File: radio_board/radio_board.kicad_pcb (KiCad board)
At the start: 2 copper layers, 61.7 x 46.5 mm, 95 parts, among them J1 3.3v, J2 GND, J3 RESET, J4 SWDCLK, J5 SWDIO, Q1 2N7002K, SW2 RKB2SJG250SMTRLFS, SW3 MSK12C02, U1 FSC-BT1036C, U2 TP4057, U3 XB5352A, U5 S2B-PH-K-S(LF)(SN), U6 TLV75533PDBVR, U7 LMV321, U8 STM32G030F6P6TR

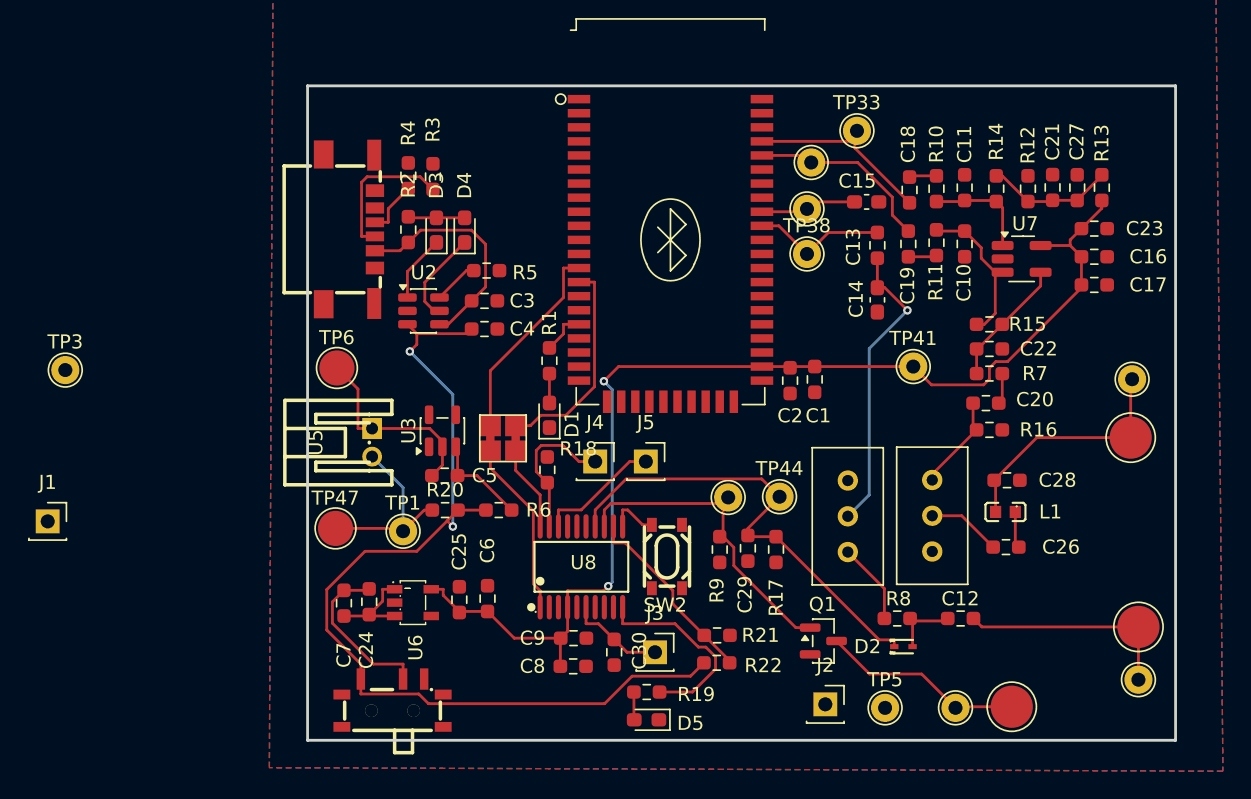
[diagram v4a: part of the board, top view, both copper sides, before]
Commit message: [Feature] Cleaned up PCB and schematics. Add logo, checked schematic, layout and wiring
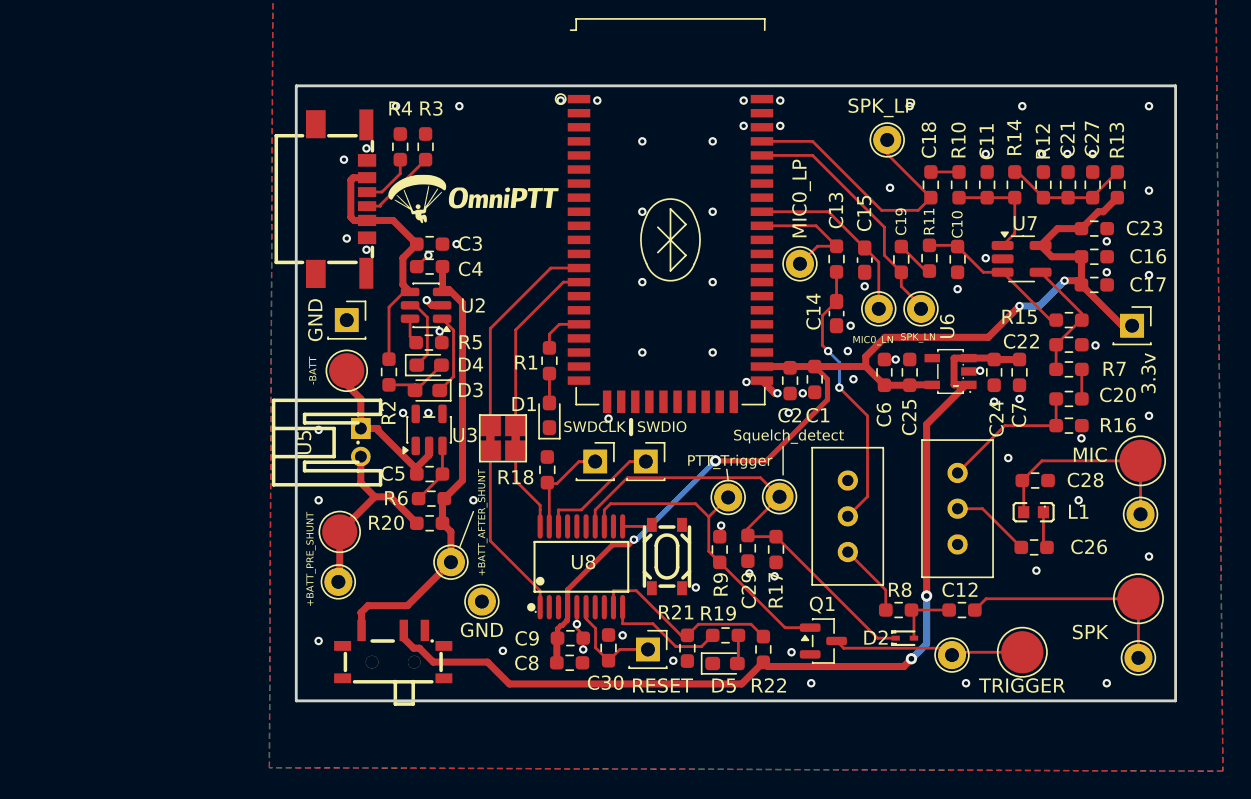
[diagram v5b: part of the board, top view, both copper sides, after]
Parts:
- removed TP41: +3.3V, TestPoint:TestPoint_THTPad_D2.0mm_Drill1.0mm
- added G***: LOGO, PTT_Project_logo:omniPTT_logo, F.Cu at (108.4, 57.0)
- C5: value 0.1uF -> 100nF
- R20: value 1 -> 0.2
- TP1: value TP_IBATT_H -> +BATT_PRE_SHUNT
- TP14, TP43: value K_CONNECTOR_PTT_TRIGGER_SLEEVE -> TRIGGER
- TP20, TP45: value K_CONNECTOR_SPK_OUT -> SPK
- TP3: value TP_IBATT_L -> +BATT_AFTER_SHUNT
- TP47: value +BATT -> +BATT_PRE_SHUNT
- TP50, TP51: value K_CONNECTOR_MIC_IN -> MIC
- moved J1 78.3 mm to (154.8, 65.6)
- moved C7 50.7 mm to (146.8, 68.9), turned to 90 degrees
- moved C24 47.3 mm to (145.0, 68.9), turned to 90 degrees
- moved J2 43.6 mm to (99.0, 65.2)
- moved U6 41.6 mm to (141.9, 68.8), turned to 0 degrees
- moved C25 35.8 mm to (139.0, 68.9)
- moved C6 32.5 mm to (137.2, 68.9)
- moved TP3 30.6 mm to (106.4, 82.4)
- moved TP5 29.6 mm to (108.6, 85.2)
- moved TP34 13.0 mm to (139.8, 64.4)
- moved D3 11.4 mm to (104.7, 70.2), turned to 180 degrees
- moved R2 10.2 mm to (102.0, 68.9), turned to -90 degrees
- moved D4 9.92 mm to (104.8, 68.4), turned to 0 degrees
- moved TP50 9.62 mm to (155.4, 79.0)
- moved TP49 8.74 mm to (136.8, 64.4)
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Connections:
- net Net-(R20-Pad1) renamed /+BATT_PRE_SHUNT
- C24 pad 1: Net-(C24-Pad1) -> GND
- C24 pad 2: Net-(U6-EN) -> +BATT_AFTER_SWITCH
- C7 pad 1: Net-(C24-Pad1) -> GND
- C7 pad 2: Net-(U6-EN) -> +BATT_AFTER_SWITCH
- R21 pad 1: GND -> Net-(U8-PA2)
- R21 pad 2: Net-(U8-PA5) -> GND
- R22 pad 1: +BATT -> +BATT_AFTER_SWITCH
- R22 pad 2: Net-(U8-PA5) -> Net-(U8-PA2)
- SW3 pad 2: Net-(C24-Pad1) -> +BATT_AFTER_SWITCH
- U6 pad 1: Net-(U6-EN) -> +BATT_AFTER_SWITCH
- U6 pad 3: Net-(U6-EN) -> +BATT_AFTER_SWITCH
- U8 pad 12: Net-(U8-PA5) -> unconnected-(U8-PA5-Pad12)
- U8 pad 9: unconnected-(U8-PA2-Pad9) -> Net-(U8-PA2)
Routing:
- net +BATT_AFTER_SWITCH: track 0.00 -> 67.7 mm, vias 0 -> 2
- net +BATT: track 68.7 -> 32.0 mm, vias 2 -> 0
- net Net-(U8-PA2): track 0.00 -> 13.8 mm
- net Net-(U8-PA5): track 13.6 -> 0.00 mm
- net Net-(C24-Pad1): track 11.8 -> 0.00 mm
- net GND: track 0.00 -> 7.95 mm, vias 0 -> 77
- net Net-(U6-EN): track 6.73 -> 0.00 mm
- net SPK_LP: track 13.4 -> 19.8 mm
- net MIC0_LN: track 6.86 -> 12.9 mm
- net Debug_gpio: track 14.3 -> 8.58 mm
- net Net-(USB1-CC2): track 10.4 -> 5.58 mm
- net SPK_LN: track 13.4 -> 17.5 mm
- net SWDCLK: track 10.6 -> 7.12 mm
- net Net-(C20-Pad2): track 6.87 -> 10.3 mm
- net 5V_usb: track 16.3 -> 19.3 mm
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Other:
- board size 61.7 x 46.5 mm -> 62.5 x 43.7 mm

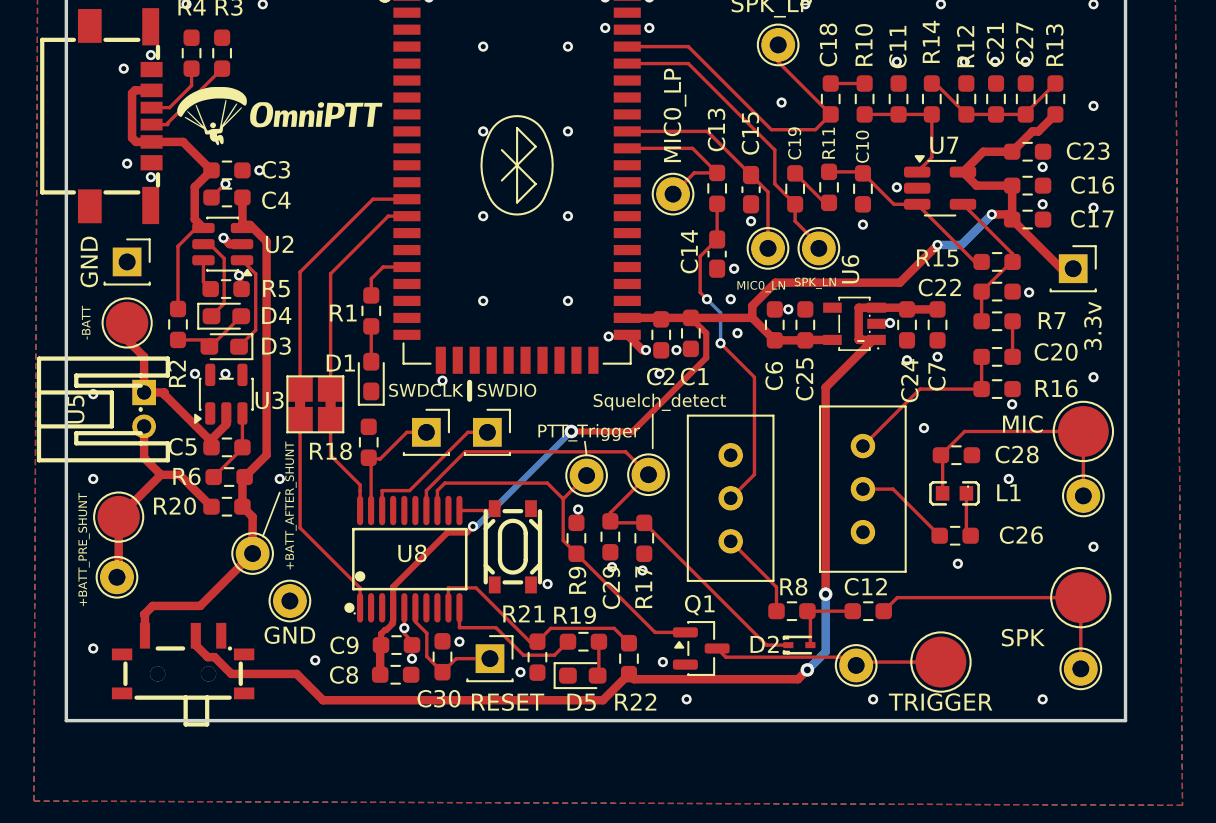
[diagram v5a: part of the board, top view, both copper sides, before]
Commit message: [Feature] Add ferrite and cap
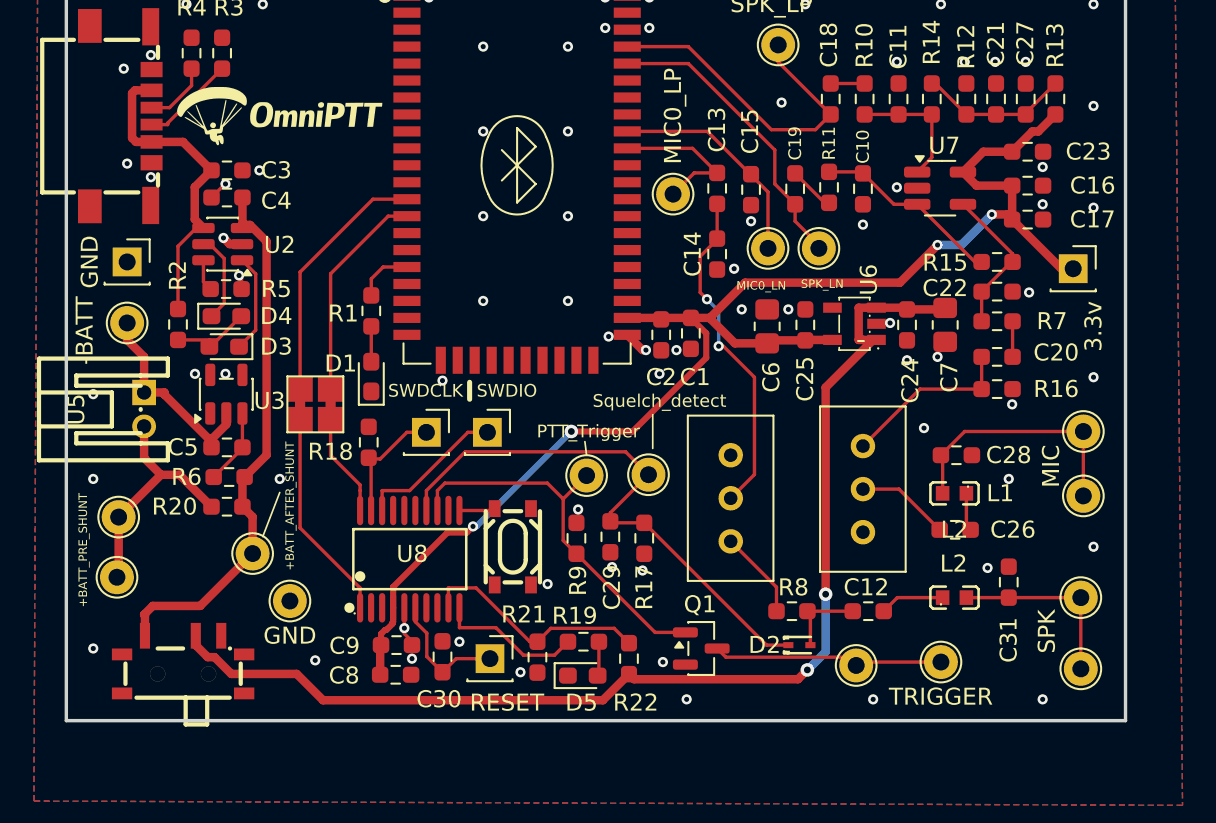
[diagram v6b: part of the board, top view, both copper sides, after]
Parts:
- added C31: 100pF, Resistor_SMD:R_0603_1608Metric_Pad0.98x0.95mm_HandSolder, F.Cu at (151.0, 84.1)
- added L2: BLM18KG601SN1D, PTT_Project_library:L0603, F.Cu at (147.8, 85.0)
- C14: value 1nF -> 47nF; footprint Capacitor_SMD:C_0603_1608Metric_Pad1.08x0.95mm_HandSolder -> Resistor_SMD:R_0603_1608Metric_Pad0.98x0.95mm_HandSolder
- C15: footprint Capacitor_SMD:C_0603_1608Metric_Pad1.08x0.95mm_HandSolder -> Resistor_SMD:R_0603_1608Metric_Pad0.98x0.95mm_HandSolder
- C28: value 1nF -> 100pF
- C6, C7: value 10uF -> 22uF; footprint Resistor_SMD:R_0603_1608Metric_Pad0.98x0.95mm_HandSolder -> Resistor_SMD:R_0805_2012Metric_Pad1.20x1.40mm_HandSolder
- J1, J2, J3, J4, J5: footprint Connector_PinSocket_2.54mm:PinSocket_1x01_P2.54mm_Vertical -> Connector_PinHeader_1.00mm:PinHeader_1x01_P1.00mm_Vertical
- TP20, TP43, TP51: footprint TestPoint:TestPoint_Pad_D3.0mm -> TestPoint:TestPoint_THTPad_D2.0mm_Drill1.0mm
- TP47, TP6: footprint TestPoint:TestPoint_Pad_D2.5mm -> TestPoint:TestPoint_THTPad_D2.0mm_Drill1.0mm
- moved C6 0.46 mm to (136.8, 69.0)
- moved C7 0.45 mm to (147.2, 68.9)
- moved C26 0.35 mm to (147.8, 81.0)
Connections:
- TP20 pad 1: Net-(C12-Pad1) -> Net-(C31-Pad2)
- TP45 pad 1: Net-(C12-Pad1) -> Net-(C31-Pad2)
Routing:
- net Net-(C12-Pad1): track 16.2 -> 3.81 mm
- net Net-(C31-Pad2): track 0.00 -> 11.0 mm
- net +3.3V: track 80.2 -> 82.4 mm
- net GND: vias 77 -> 76

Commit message: [Milestone] Last commit before pourchasing v2
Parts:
- removed C23: 33 pF, Resistor_SMD:R_0603_1608Metric_Pad0.98x0.95mm_HandSolder
- C10, C11, C22: value 33 pF -> 33pF
- C16: value 100 nF -> 100nF
- J1, J2, J3, J4, J5: footprint Connector_PinHeader_1.00mm:PinHeader_1x01_P1.00mm_Vertical -> Connector_PinHeader_2.54mm:PinHeader_1x01_P2.54mm_Vertical
- moved G*** 0.52 mm to (107.9, 57.1)
- moved J5 0.25 mm to (120.5, 75.2)
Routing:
- net GND: track 7.95 -> 9.17 mm
